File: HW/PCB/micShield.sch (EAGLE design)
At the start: 19 parts, among them U2 LT6002CGN

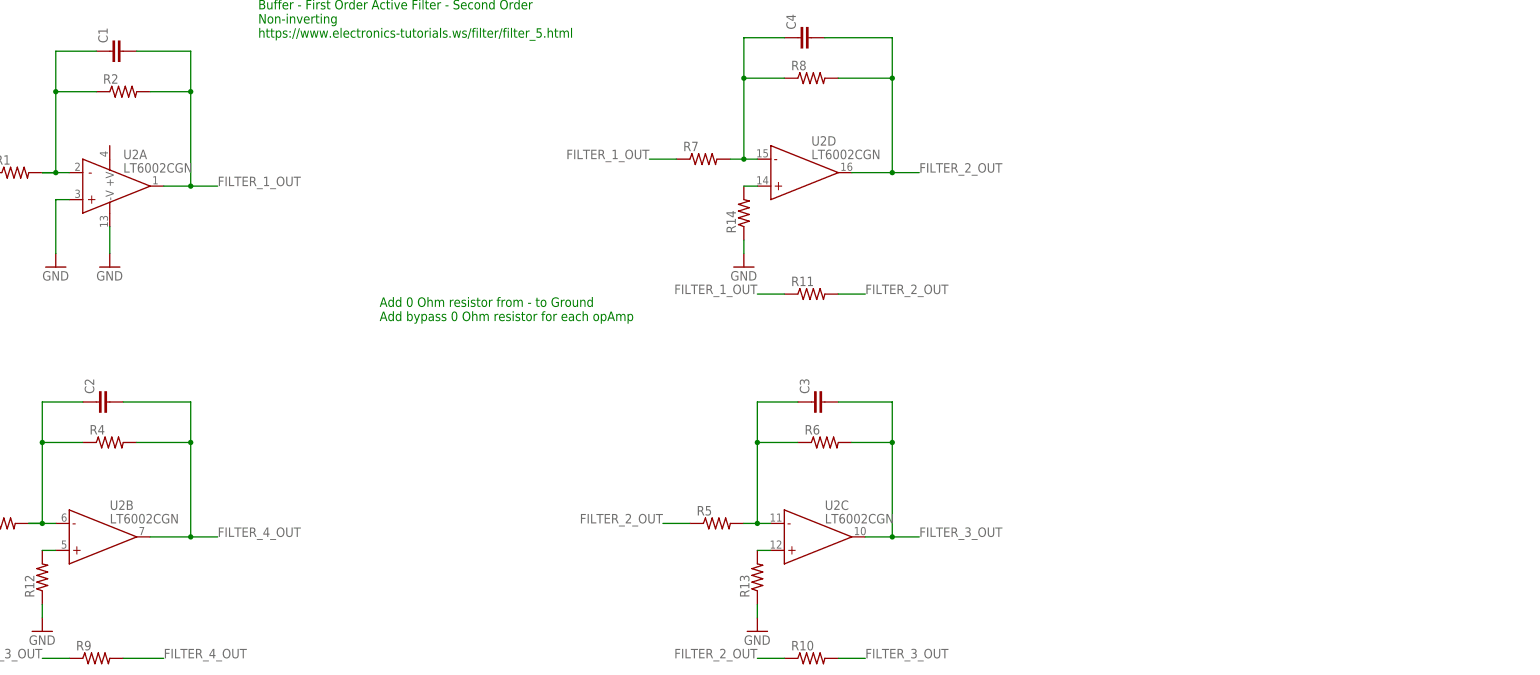
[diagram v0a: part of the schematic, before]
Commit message: Added Mic Library and updates to PCB.
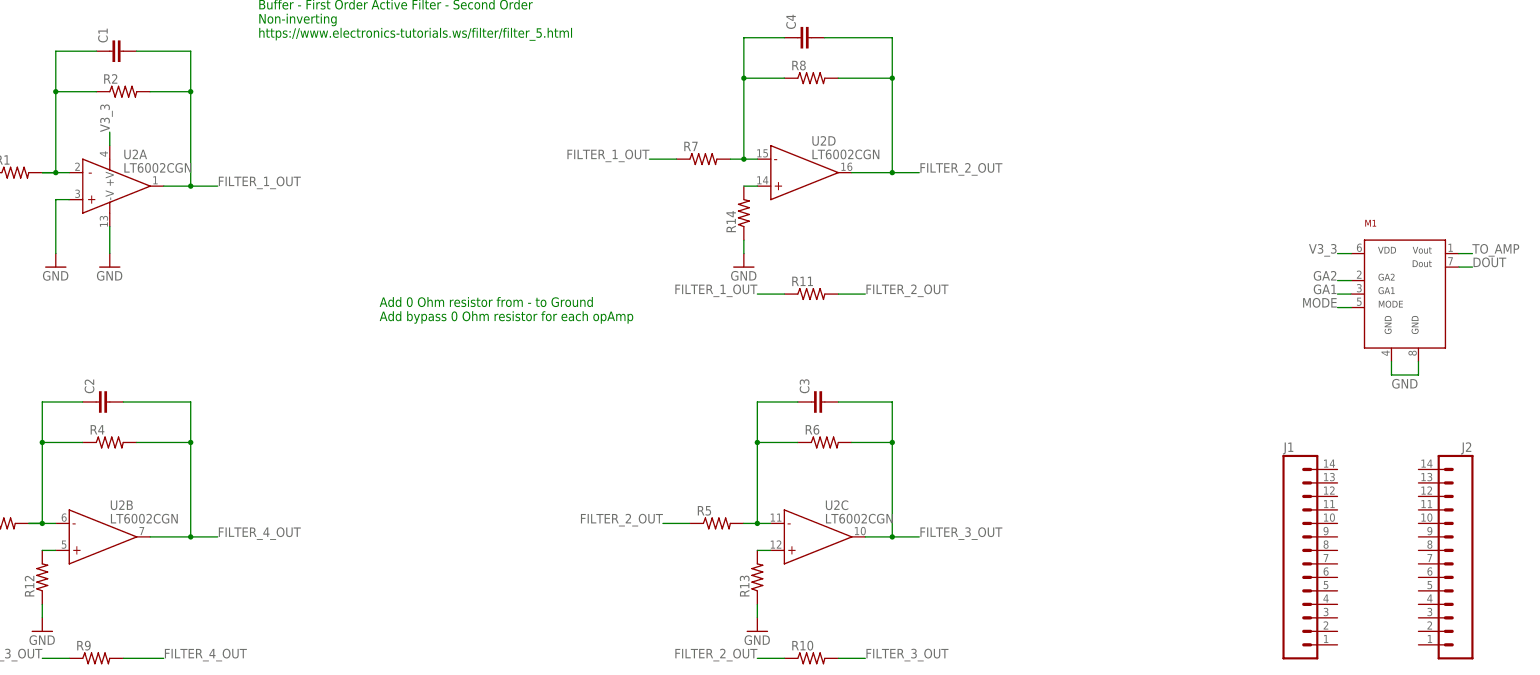
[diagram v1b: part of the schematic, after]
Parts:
- added J1, J2: (no value), SparkFun-Connectors:M14
- added M1: PMM-3738-VM1010-R, MIC:PMM-3738-VM1010-R
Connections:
- new net DOUT: M1.P$7
- new net GA1: M1.P$3
- new net GA2: M1.P$2
- new net MODE: M1.P$5
- new net V3_3: M1.P$6, U2A.+V
- net GND: now also M1.P$4, M1.P$8
- net TO_AMP: now also M1.P$1
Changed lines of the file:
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@@
 <layer number="112" name="tSilk" color="7" fill="1" visible="yes" active="yes"/>
 <layer number="113" name="IDFDebug" color="7" fill="1" visible="yes" active="yes"/>
+<layer number="114" name="Badge_Outline" color="7" fill="1" visible="yes" active="yes"/>
+<layer number="115" name="ReferenceISLANDS" color="7" fill="1" visible="yes" active="yes"/>
 <layer number="116" name="Patch_BOT" color="9" fill="4" visible="yes" active="yes"/>
 <layer number="118" name="Rect_Pads" color="7" fill="1" visible="yes" active="yes"/>
@@
 <part name="R13" library="SparkFun-Passives" deviceset="RESISTOR" device="0603-RES"/>
 <part name="R14" library="SparkFun-Passives" deviceset="RESISTOR" device="0603-RES"/>
+<part name="M1" library="MIC" deviceset="PMM-3738-VM1010-R" device=""/>
+<part name="J1" library="SparkFun-Connectors" deviceset="M14" device=""/>
+<part name="J2" library="SparkFun-Connectors" deviceset="M14" device=""/>
 </parts>
 <sheets>
@@
 <instance part="R13" gate="G$1" x="149.86" y="-12.7" rot="R90"/>
 <instance part="R14" gate="G$1" x="147.32" y="55.88" rot="R90"/>
+<instance part="M1" gate="A" x="271.78" y="40.64"/>
+<instance part="J1" gate="G$1" x="248.92" y="-7.62"/>
+<instance part="J2" gate="G$1" x="284.48" y="-7.62" rot="MR0"/>
 </instances>
 <busses>
@@
 <wire x1="147.32" y1="50.8" x2="147.32" y2="48.26" width="0.1524" layer="91"/>
 </segment>
+<segment>
+<pinref part="M1" gate="A" pin="P$4"/>
+<wire x1="269.24" y1="27.94" x2="269.24" y2="25.4" width="0.1524" layer="91"/>
+<wire x1="269.24" y1="25.4" x2="274.32" y2="25.4" width="0.1524" layer="91"/>
+<pinref part="M1" gate="A" pin="P$8"/>
+<wire x1="274.32" y1="25.4" x2="274.32" y2="27.94" width="0.1524" layer="91"/>
+<label x="269.24" y="22.86" size="1.778" layer="95"/>
+</segment>
 </net>
 <net name="N$3" class="0">
@@
 <label x="0" y="63.5" size="1.778" layer="95" rot="MR0"/>
 </segment>
+<segment>
+<pinref part="M1" gate="A" pin="P$1"/>
+<wire x1="281.94" y1="48.26" x2="284.48" y2="48.26" width="0.1524" layer="91"/>
+<label x="284.48" y="48.26" size="1.778" layer="95"/>
+</segment>
 </net>
 <net name="FILTER_4_OUT" class="0">
@@
 </segment>
 </net>
+<net name="MODE" class="0">
+<segment>
+<pinref part="M1" gate="A" pin="P$5"/>
+<wire x1="261.62" y1="38.1" x2="259.08" y2="38.1" width="0.1524" layer="91"/>
+<label x="259.08" y="38.1" size="1.778" layer="95" rot="MR0"/>
+</segment>
+</net>
+<net name="GA1" class="0">
+<segment>
+<pinref part="M1" gate="A" pin="P$3"/>
+<wire x1="261.62" y1="40.64" x2="259.08" y2="40.64" width="0.1524" layer="91"/>
+<label x="259.08" y="40.64" size="1.778" layer="95" rot="MR0"/>
+</segment>
+</net>
+<net name="GA2" class="0">
+<segment>
+<pinref part="M1" gate="A" pin="P$2"/>
+<wire x1="261.62" y1="43.18" x2="259.08" y2="43.18" width="0.1524" layer="91"/>
+<label x="259.08" y="43.18" size="1.778" layer="95" rot="MR0"/>
+</segment>
+</net>
+<net name="V3_3" class="0">
+<segment>
+<pinref part="M1" gate="A" pin="P$6"/>
+<wire x1="261.62" y1="48.26" x2="259.08" y2="48.26" width="0.1524" layer="91"/>
+<label x="259.08" y="48.26" size="1.778" layer="95" rot="MR0"/>
+</segment>
+<segment>
+<pinref part="U2" gate="A" pin="+V"/>
+<wire x1="27.94" y1="68.58" x2="27.94" y2="71.12" width="0.1524" layer="91"/>
+<label x="27.94" y="71.12" size="1.778" layer="95" rot="R90"/>
+</segment>
+</net>
+<net name="DOUT" class="0">
+<segment>
+<pinref part="M1" gate="A" pin="P$7"/>
+<wire x1="281.94" y1="45.72" x2="284.48" y2="45.72" width="0.1524" layer="91"/>
+<label x="284.48" y="45.72" size="1.778" layer="95"/>
+</segment>
+</net>

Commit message: Adding libs. Working on analog front end.
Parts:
- removed C2, C3: (no value), SparkFun-Capacitors:CAP0603-CAP
- removed J1, J2: (no value), SparkFun-Connectors:M14
- removed R10, R12, R13, R3, R4, R5, R6, R9: (no value), SparkFun-Passives:RESISTOR0603-RES
- added C5: (no value), SparkFun-Capacitors:CAP0603-CAP
- added C6: 0.1uF, SparkFun-Capacitors:CAP0402-CAP
- added C7: 0,1uF, SparkFun-Capacitors:CAP0402-CAP
- added R15, R16, R17: (no value), SparkFun-Resistors:RESISTOR0402
- added R18, R22, R24, R28, R30: DNP, SparkFun-Resistors:RESISTOR0402
- added R19, R20, R25, R26, R31: 0, SparkFun-Resistors:RESISTOR0402
- added R21, R27: 3.9k, SparkFun-Resistors:RESISTOR0402
- added R23, R29: 3k, SparkFun-Resistors:RESISTOR0402
- added U$1: TEENSY_3.5/3.6_BASIC, Teensy356:TEENSY_3.5/3.6_BASIC
- added U1: LM27762DSSR, LM27762DSSR:LM27762DSSR
- C4: value (none) -> 0.1uF; device SparkFun-Capacitors:CAP0603-CAP -> SparkFun-Capacitors:CAP0402-CAP
- R1, R2: device SparkFun-Passives:RESISTOR0603-RES -> SparkFun-Resistors:RESISTOR0402
- R11: value (none) -> DNP; device SparkFun-Passives:RESISTOR0603-RES -> SparkFun-Resistors:RESISTOR0402
- R14: value (none) -> 3k; device SparkFun-Passives:RESISTOR0603-RES -> SparkFun-Resistors:RESISTOR0402
- R7: value (none) -> 0; device SparkFun-Passives:RESISTOR0603-RES -> SparkFun-Resistors:RESISTOR0402
- R8: value (none) -> 3.9k; device SparkFun-Passives:RESISTOR0603-RES -> SparkFun-Resistors:RESISTOR0402
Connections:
- removed net FILTER_1_OUT: C1.2, R11.1, R2.2, R7.1, U2A.OUT
- removed net FILTER_2_OUT: C4.2, R10.1, R11.2, R5.1, R8.2, U2D.OUT
- removed net FILTER_3_OUT: C3.2, R10.2, R3.1, R6.2, R9.1, U2C.OUT
- removed net FILTER_4_OUT: C2.2, R4.2, R9.2, U2B.OUT
- removed net N$2: R12.2, U2B.+IN
- removed net N$3: C2.1, R3.2, R4.1, U2B.-IN
- removed net N$4: R13.2, U2C.+IN
- removed net N$5: C3.1, R5.2, R6.1, U2C.-IN
- removed net N$8: R14.2, U2D.+IN
- removed net V3_3: M1.P$6, U2A.+V
- new net F1_OUT: R11.2, R19.2, R26.1, R28.1
- new net F2_OUT: R20.1, R22.1, R28.2, R31.2
- new net FILTERED_OUT: R22.2, R25.2
- new net N$10: C4.2, R19.1, R8.2, U2D.OUT
- new net N$12: R20.2, R24.2, U2C.-IN
- new net N$13: C6.1, R21.1, R23.2, U2C.+IN
- new net N$14: C6.2, R21.2, R25.1, U2C.OUT
- new net N$16: R26.2, R30.2, U2B.-IN
- new net N$17: C7.1, R27.1, R29.2, U2B.+IN
- new net N$18: C7.2, R27.2, R31.1, U2B.OUT
- new net N$6: R15.2, R16.1, R17.1, U2A.+IN
- new net N$9: R18.2, R7.2, U2D.+IN
- new net OFFSET_REMOVED: R11.1, R2.2, R7.1, U2A.OUT
- new net V3_3N: C1.1, U2A.-V
- new net V3_3P: C5.1, M1.P$6, R15.1, U2A.+V
- net GND: now also C1.2, C5.2, R16.2, R17.2, R18.1, R23.1, R24.1, R29.1, R30.1; no longer R12.1, R13.1, U2A.+IN, U2A.-V
- net N$1: no longer C1.1
- net N$7: now also R14.2; no longer R7.2
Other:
- note added: "3k - P3.0KDBCT-ND 3.9k - P3.9KDBCT-ND"
- note added: "LM2776 Needs thermal pad grounded"
- note removed: "Add 0 Ohm resistor from - to Ground Add bypass 0 Ohm resistor for each opAmp"
